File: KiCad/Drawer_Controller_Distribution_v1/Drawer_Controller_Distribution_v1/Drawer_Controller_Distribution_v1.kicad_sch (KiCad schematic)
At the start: 2 parts, among them J1 RJ45 (6339160-1)

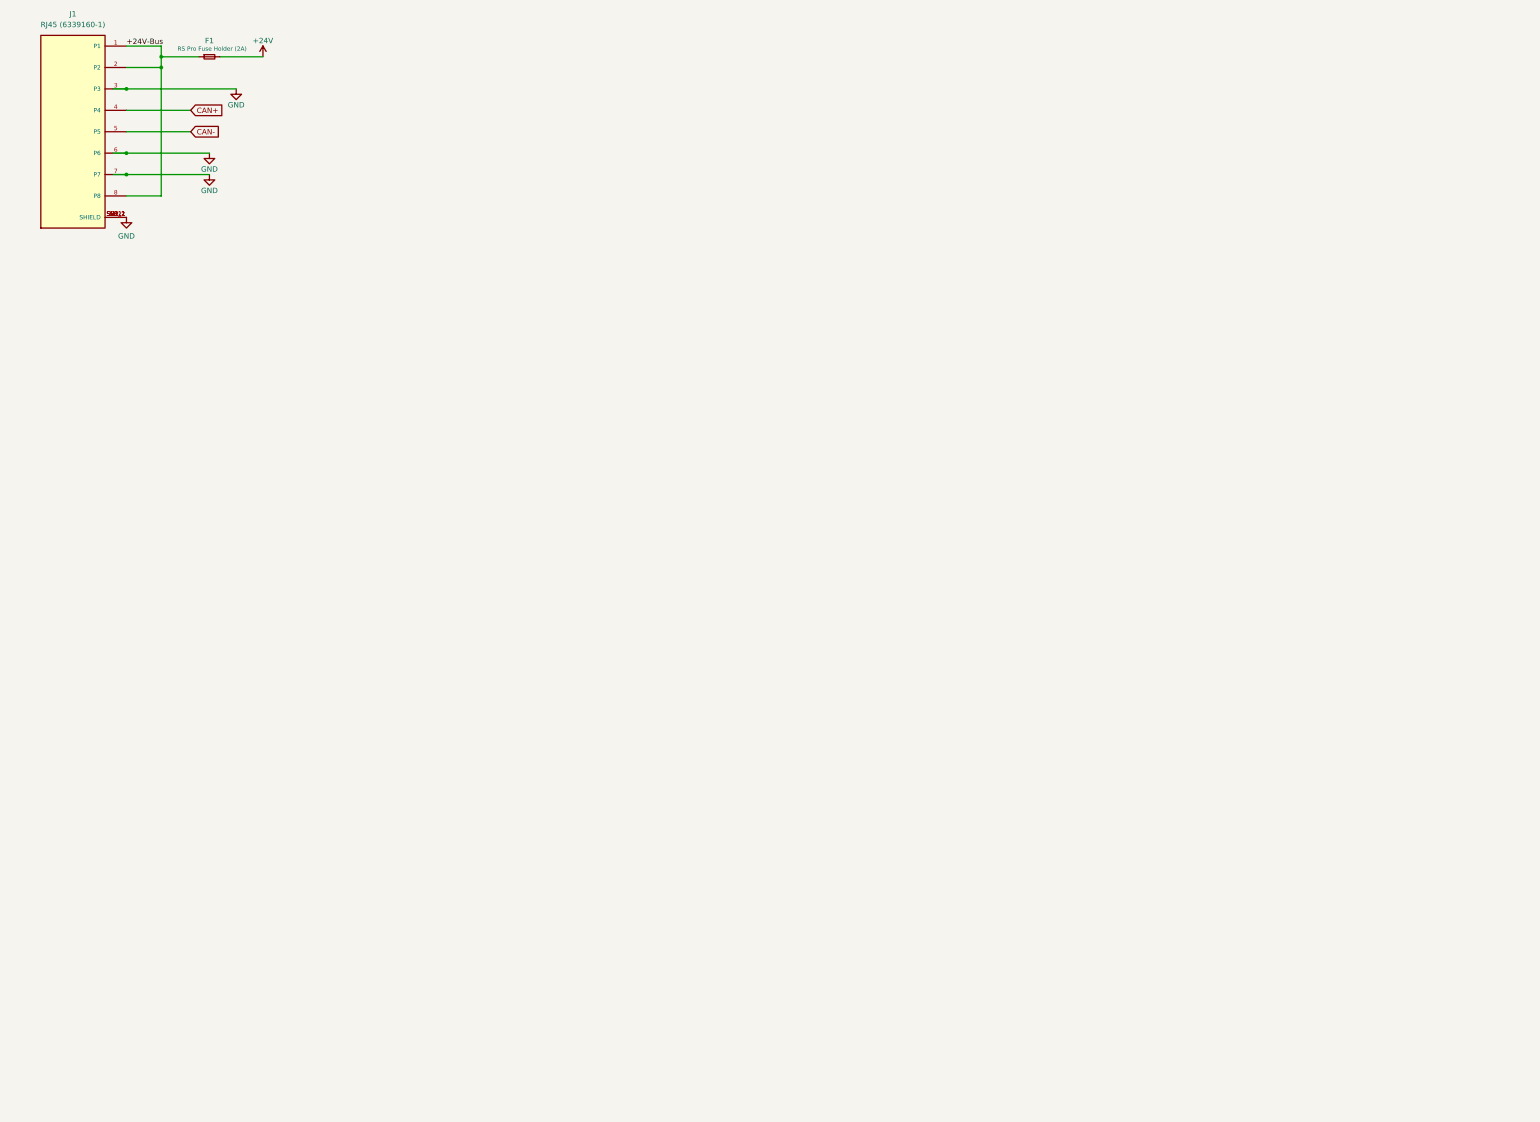
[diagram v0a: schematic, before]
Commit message: Progress in design of drawer controller distribution board
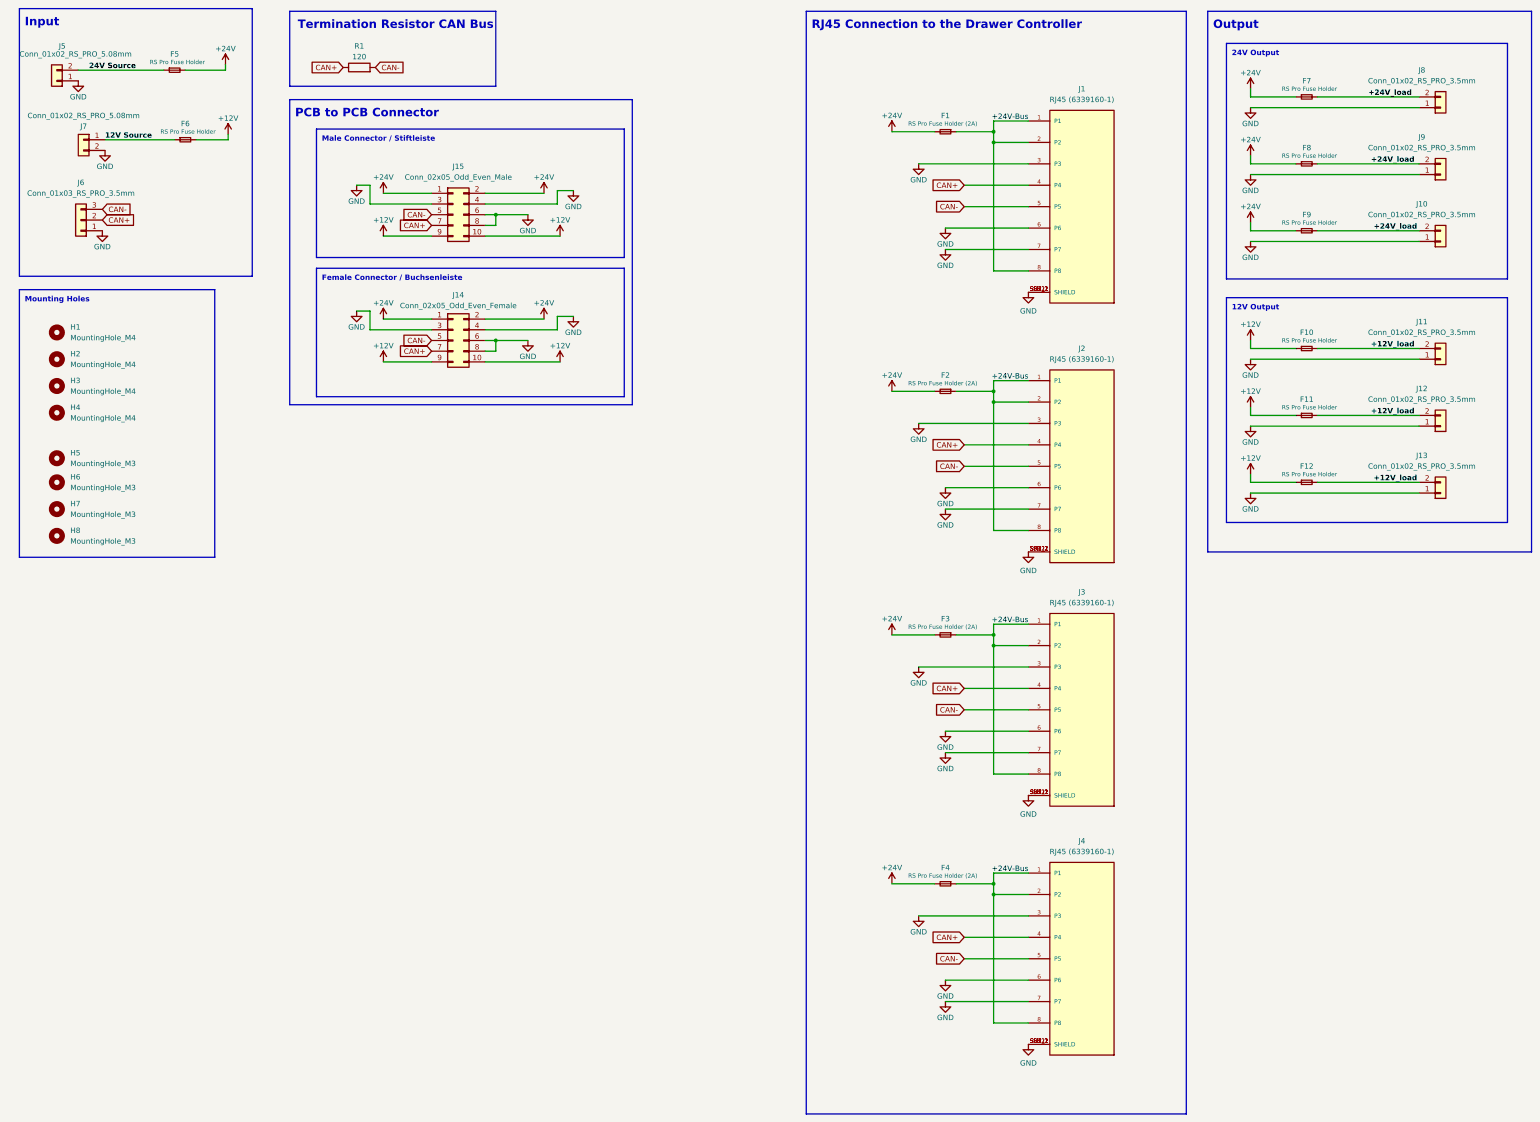
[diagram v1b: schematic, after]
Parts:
- added F10, F11, F12, F5, F6, F7, F8, F9: RS Pro Fuse Holder, Robast_Footprints:Fuse_Holder_RS_Pro_188-4477, symbol Device:Fuse_Small
- added F2, F3, F4: RS Pro Fuse Holder (2A), Robast_Footprints:Fuse_Holder_RS_Pro_188-4477, symbol Device:Fuse_Small
- added H1, H2, H3, H4: MountingHole_M4, MountingHole:MountingHole_4.3mm_M4, symbol Mechanical:MountingHole
- added H5, H6, H7, H8: MountingHole_M3, MountingHole:MountingHole_3.2mm_M3, symbol Mechanical:MountingHole
- added J10, J11, J12, J13, J8, J9: Conn_01x02_RS_PRO_3.5mm, Connector_Phoenix_MC:PhoenixContact_MC_1,5_2-G-3.5_1x02_P3.50mm_Horizontal, symbol Connector_Generic:Conn_01x02
- added J14: Conn_02x05_Odd_Even_Female, Connector_PinSocket_2.54mm:PinSocket_2x05_P2.54mm_Horizontal, symbol Connector_Generic:Conn_02x05_Odd_Even
- added J15: Conn_02x05_Odd_Even_Male, Connector_PinHeader_2.54mm:PinHeader_2x05_P2.54mm_Horizontal, symbol Connector_Generic:Conn_02x05_Odd_Even
- added J2, J3, J4: RJ45 (6339160-1), Robast_Footprints:TE_6339160-1, symbol 6339160-1:6339160-1
- added J5, J7: Conn_01x02_RS_PRO_5.08mm, Connector_Phoenix_MSTB:PhoenixContact_MSTBA_2,5_2-G-5,08_1x02_P5.08mm_Horizontal, symbol Connector_Generic:Conn_01x02
- added J6: Conn_01x03_RS_PRO_3.5mm, Connector_Phoenix_MC:PhoenixContact_MC_1,5_3-G-3.5_1x03_P3.50mm_Horizontal, symbol Connector_Generic:Conn_01x03
- added R1: 120, Resistor_SMD:R_0805_2012Metric, symbol Device:R
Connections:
- net +24V: now also F2.2, F3.2, F4.2, F5.2, F7.1, F8.1, F9.1, J14.1 (Pin_1), J14.2 (Pin_2), J15.1 (Pin_1), J15.2 (Pin_2)
- net +24V-Bus: now also F2.1, F3.1, F4.1, J2.1 (P1), J2.2 (P2), J2.8 (P8), J3.1 (P1), J3.2 (P2), J3.8 (P8), J4.1 (P1), J4.2 (P2), J4.8 (P8)
- net CAN+: now also J14.7 (Pin_7), J15.7 (Pin_7), J2.4 (P4), J3.4 (P4), J4.4 (P4), J6.2 (Pin_2), R1.1
- net CAN-: now also J14.5 (Pin_5), J15.5 (Pin_5), J2.5 (P5), J3.5 (P5), J4.5 (P5), J6.3 (Pin_3), R1.2
- net GND: now also J10.1 (Pin_1), J11.1 (Pin_1), J12.1 (Pin_1), J13.1 (Pin_1), J14.3 (Pin_3), J14.4 (Pin_4), J14.6 (Pin_6), J14.8 (Pin_8), J15.3 (Pin_3), J15.4 (Pin_4), J15.6 (Pin_6), J15.8 (Pin_8), J2.3 (P3), J2.6 (P6), J2.7 (P7), J2.SH1 (SHIELD), J2.SH1_1 (SHIELD), J2.SH1_2 (SHIELD), J2.SH2 (SHIELD), J2.SH2_1 (SHIELD), J2.SH2_2 (SHIELD), J3.3 (P3), J3.6 (P6), J3.7 (P7), J3.SH1 (SHIELD), J3.SH1_1 (SHIELD), J3.SH1_2 (SHIELD), J3.SH2 (SHIELD), J3.SH2_1 (SHIELD), J3.SH2_2 (SHIELD), J4.3 (P3), J4.6 (P6), J4.7 (P7), J4.SH1 (SHIELD), J4.SH1_1 (SHIELD), J4.SH1_2 (SHIELD), J4.SH2 (SHIELD), J4.SH2_1 (SHIELD), J4.SH2_2 (SHIELD), J5.1 (Pin_1), J6.1 (Pin_1), J7.2 (Pin_2), J8.1 (Pin_1), J9.1 (Pin_1)
- new net +12V: F10.1, F11.1, F12.1, F6.2, J14.10 (Pin_10), J14.9 (Pin_9), J15.10 (Pin_10), J15.9 (Pin_9)
- new net +12V_load: F10.2, F11.2, F12.2, J11.2 (Pin_2), J12.2 (Pin_2), J13.2 (Pin_2)
- new net +24V_load: F7.2, F8.2, F9.2, J10.2 (Pin_2), J8.2 (Pin_2), J9.2 (Pin_2)
- new net 12V Source: F6.1, J7.1 (Pin_1)
- new net 24V Source: F5.1, J5.2 (Pin_2)
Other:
- note added: "12V Output"
- note added: "24V Output"
- note added: "Female Connector / Buchsenleiste"
- note added: "Input"
- note added: "Male Connector / Stiftleiste"
- note added: "Mounting Holes"
- note added: "Output"
- note added: "PCB to PCB Connector"
- note added: "RJ45 Connection to the Drawer Controller"
- note added: "Termination Resistor CAN Bus"
- moved on the sheet: F1, J1

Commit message: Finalizing drawer controller distribution board an creating files for the pcb order
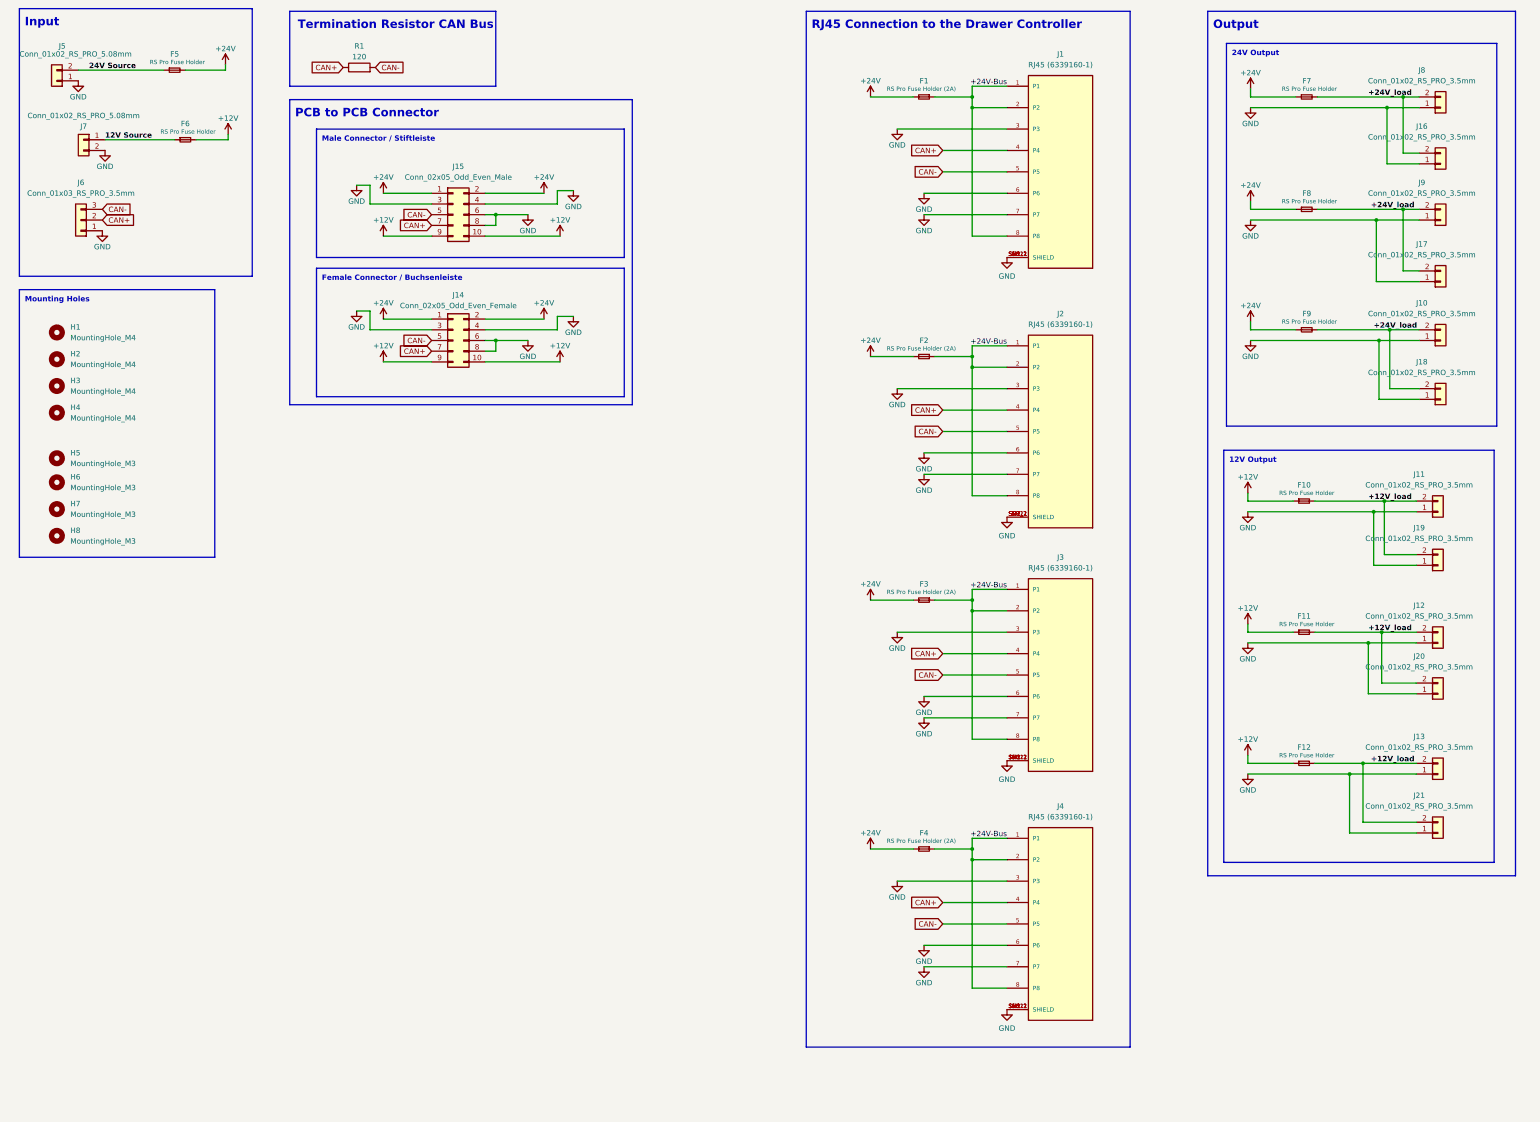
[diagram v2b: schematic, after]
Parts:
- added J16, J17, J18, J19, J20, J21: Conn_01x02_RS_PRO_3.5mm, Connector_Phoenix_MC:PhoenixContact_MC_1,5_2-G-3.5_1x02_P3.50mm_Horizontal, symbol Connector_Generic:Conn_01x02
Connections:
- net +12V_load: now also J19.2 (Pin_2), J20.2 (Pin_2), J21.2 (Pin_2)
- net +24V_load: now also J16.2 (Pin_2), J17.2 (Pin_2), J18.2 (Pin_2)
- net GND: now also J16.1 (Pin_1), J17.1 (Pin_1), J18.1 (Pin_1), J19.1 (Pin_1), J20.1 (Pin_1), J21.1 (Pin_1)
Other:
- moved on the sheet: F1, F10, F11, F12, F2, F3, F4, F8, F9, J1, J10, J11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
